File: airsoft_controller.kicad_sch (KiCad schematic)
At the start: 37 parts, among them J1 Conn_01x07, J2 Conn_01x03, J3 Conn_01x03, J4 Conn_01x01, J5 Conn_01x03, J6 Micro_SD_Card, J7 Conn_01x03, J8 Conn_01x02, SW1 MEMBRANE, SW2 MEMBRANE, SW3 MECH_SW, SW4 MEMBRANE, SW5 MEMBRANE, SW6 MEMBRANE, SW7 MEMBRANE, U1 CP2102N-Axx-xQFN20, U2 ESP32-S3-WROOM-1, U3 74HC595, U4 SN74HCS165

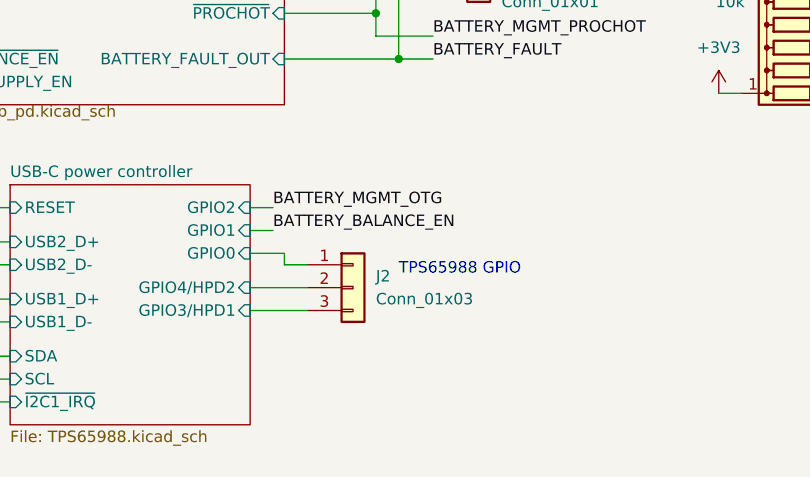
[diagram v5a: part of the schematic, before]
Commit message: edited usb pcb part
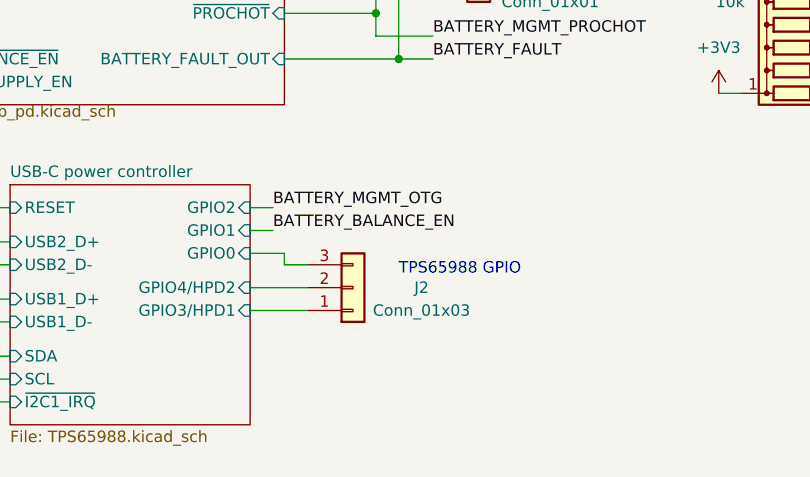
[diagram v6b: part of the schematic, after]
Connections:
- net USB-C power controller/GPIO0: now also J2.3 (Pin_3); no longer J2.1 (Pin_1)
- net USB-C power controller/GPIO3/HPD1: now also J2.1 (Pin_1); no longer J2.3 (Pin_3)
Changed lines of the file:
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@@
     (pin "1")
   )
-  (symbol (lib_id "Connector_Generic:Conn_01x03") (at 151.13 177.8 0) (unit 1)
-    (in_bom yes) (on_board yes) (fields_autoplaced)
-    (property "Reference" "J2" (id 0) (at 153.67 176.5299 0)
-      (effects (font (size 1.27 1.27)) (justify left))
-    )
-    (property "Value" "Conn_01x03" (id 1) (at 153.67 179.0699 0)
-      (effects (font (size 1.27 1.27)) (justify left))
-    )
+  (symbol (lib_id "Connector_Generic:Conn_01x03") (at 151.13 177.8 0) (mirror x) (unit 1)
+    (in_bom yes) (on_board yes)
+    (property "Reference" "J2" (id 0) (at 158.75 177.8 0))
+    (property "Value" "Conn_01x03" (id 1) (at 158.75 180.34 0))
     (property "Footprint" "Connector_PinSocket_2.54mm:PinSocket_1x03_P2.54mm_Vertical" (id 2) (at 151.13 177.8 0)
       (effects (font (size 1.27 1.27)) hide)
@@
     )
     (path "/dad78a3c-8763-4d20-b96b-942d6d484c24/f36f53a9-1291-4e1f-b242-7f104e919722"
-      (reference "C88") (unit 1) (value "10uF") (footprint "Capacitor_SMD:C_1206_3216Metric_Pad1.33x1.80mm_HandSolder")
+      (reference "C88") (unit 1) (value "10uF") (footprint "Capacitor_SMD:C_0805_2012Metric_Pad1.18x1.45mm_HandSolder")
     )
     (path "/dad78a3c-8763-4d20-b96b-942d6d484c24/d1db56bf-3f0a-4c29-8d97-5c6c3b7f42b1"
@@
     )
     (path "/dad78a3c-8763-4d20-b96b-942d6d484c24/7aaff0ab-8327-4583-8203-10eca9c35982"
-      (reference "C97") (unit 1) (value "10uF") (footprint "Capacitor_SMD:C_1206_3216Metric_Pad1.33x1.80mm_HandSolder")
+      (reference "C97") (unit 1) (value "10uF") (footprint "Capacitor_SMD:C_0805_2012Metric_Pad1.18x1.45mm_HandSolder")
     )
     (path "/dad78a3c-8763-4d20-b96b-942d6d484c24/4cd178db-9321-4997-91c7-f4d92beaf346"
@@
       (reference "C161") (unit 1) (value "22uF") (footprint "Capacitor_SMD:CP_Elec_5x5.3")
     )
+    (path "/dad78a3c-8763-4d20-b96b-942d6d484c24/2c870a98-ce2d-4021-953b-e874aa1f6f56"
+      (reference "C162") (unit 1) (value "4.7uF") (footprint "Capacitor_SMD:C_0603_1608Metric_Pad1.08x0.95mm_HandSolder")
+    )
     (path "/8ab84ef1-8252-469c-850a-9e4f14e4ddfd/384718a6-59f9-40f6-8b54-45db59321c91"

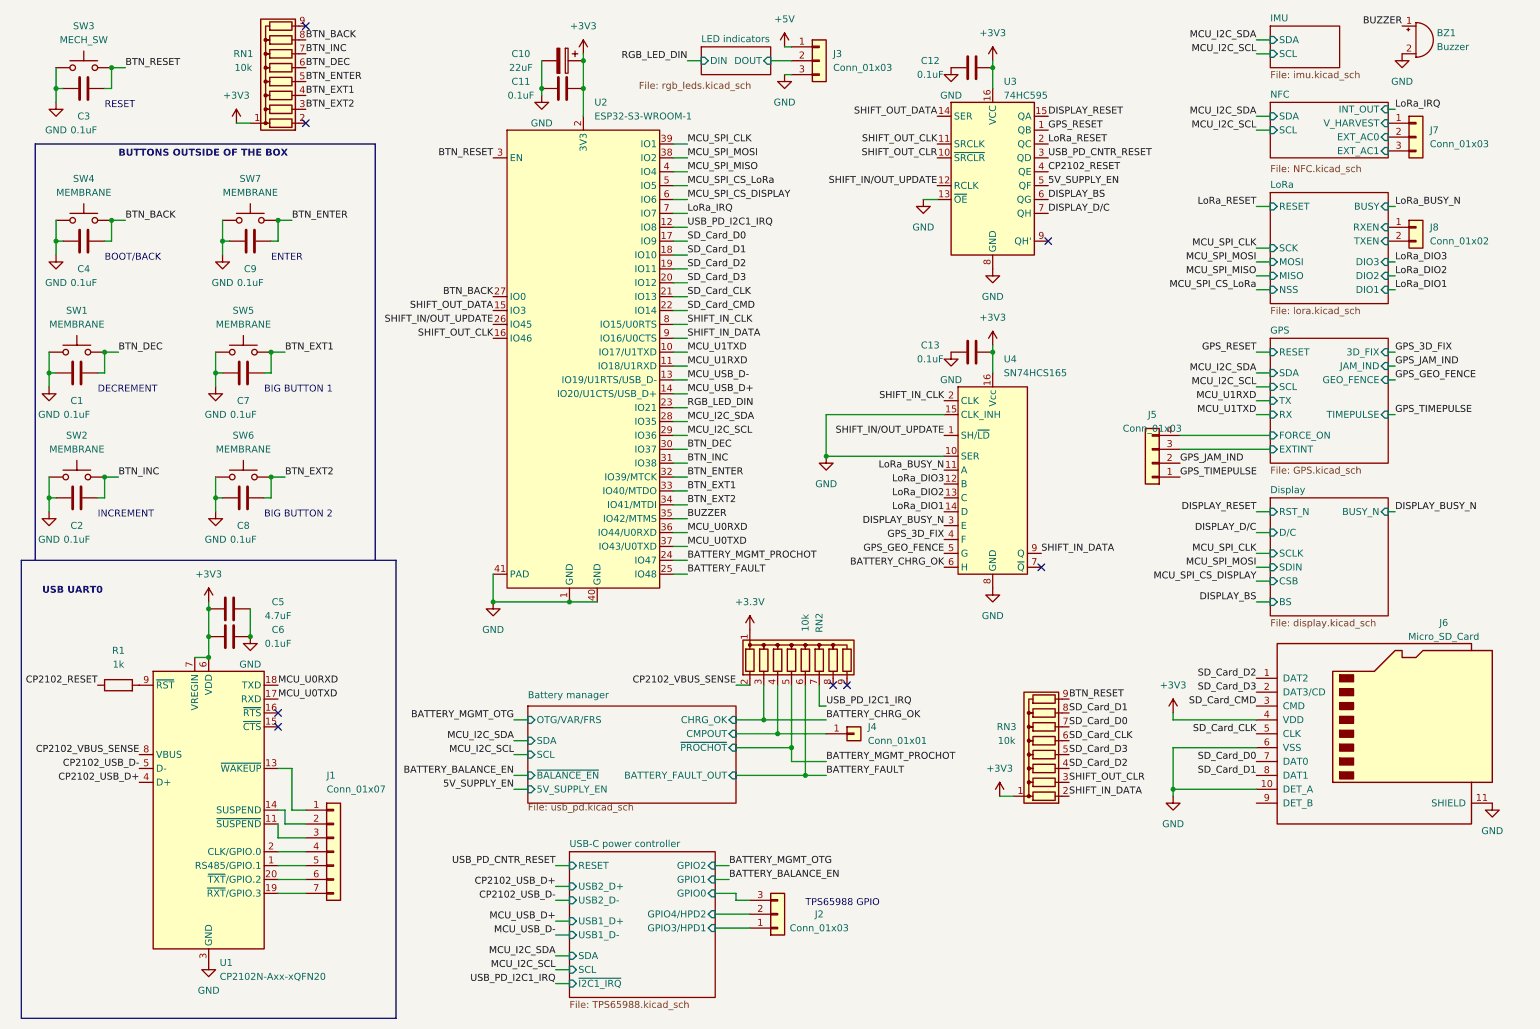
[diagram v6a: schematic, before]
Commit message: usb power source added, need to reassemble to 4-layers
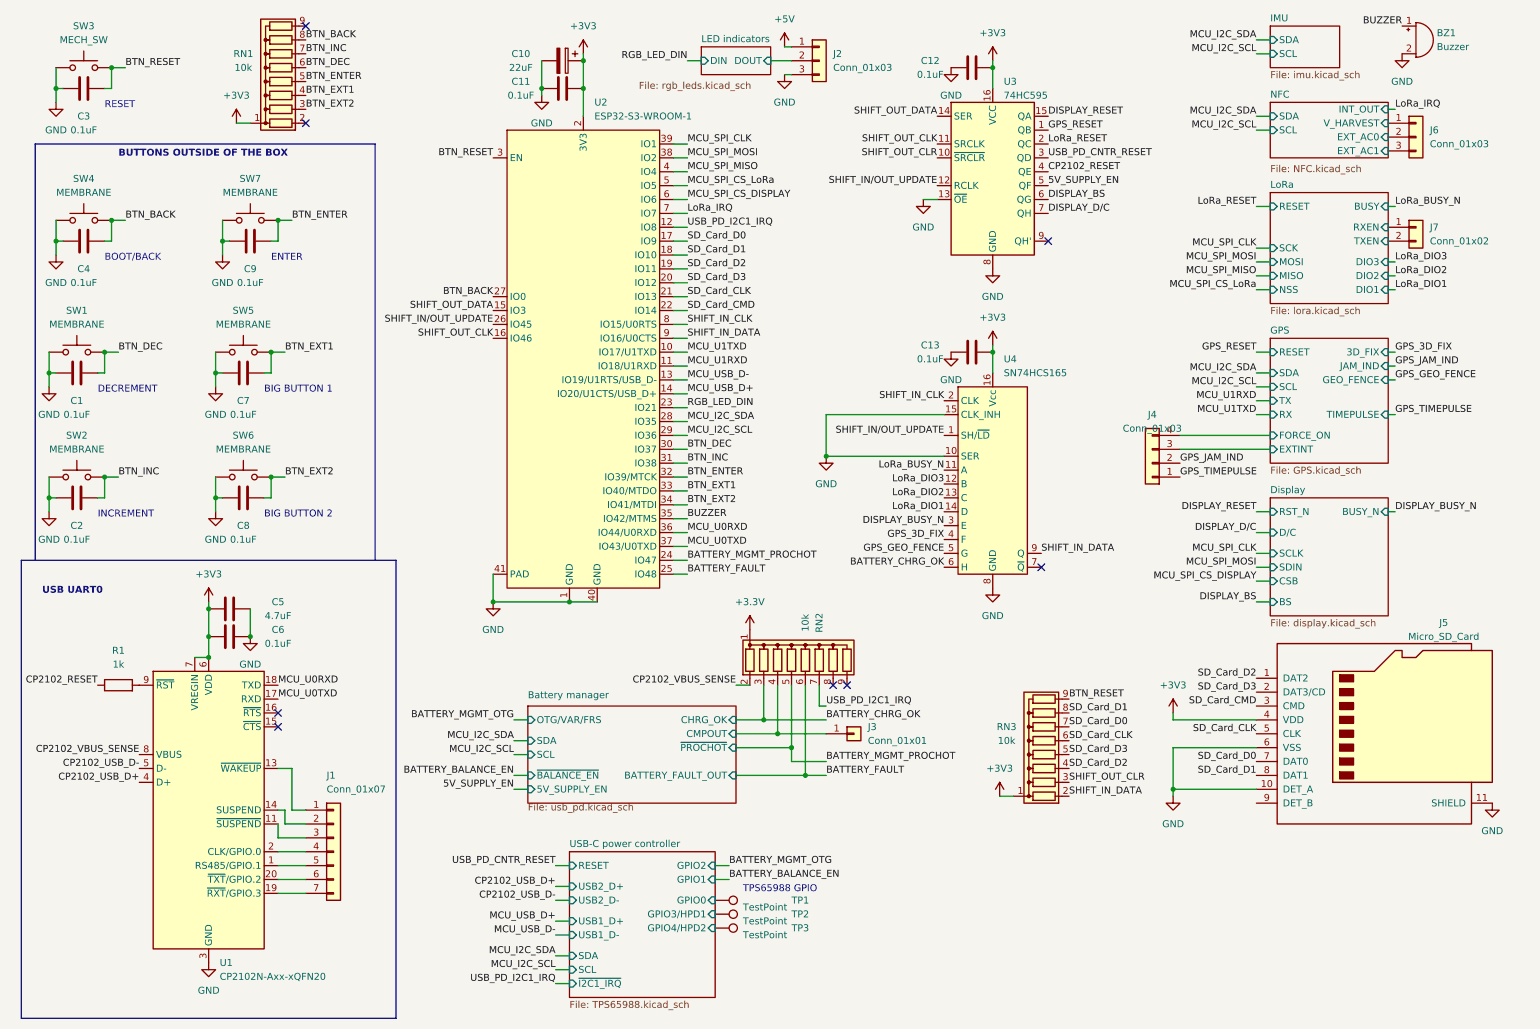
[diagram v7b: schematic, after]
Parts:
- removed J2: Conn_01x03, Connector_PinSocket_2.54mm:PinSocket_1x03_P2.54mm_Vertical, symbol Connector_Generic:Conn_01x03
- added TP1, TP2, TP3: TestPoint, TestPoint:TestPoint_Pad_D1.5mm, symbol Connector:TestPoint
- renumbered J3 to J2, J4 to J3, J5 to J4, J6 to J5, J7 to J6, J8 to J7
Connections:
- net USB-C power controller/GPIO0: now also TP1.1
- net USB-C power controller/GPIO3/HPD1: now also TP2.1
- net USB-C power controller/GPIO4/HPD2: now also TP3.1

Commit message: done first iteration of pcb routing, slikscreen still broken
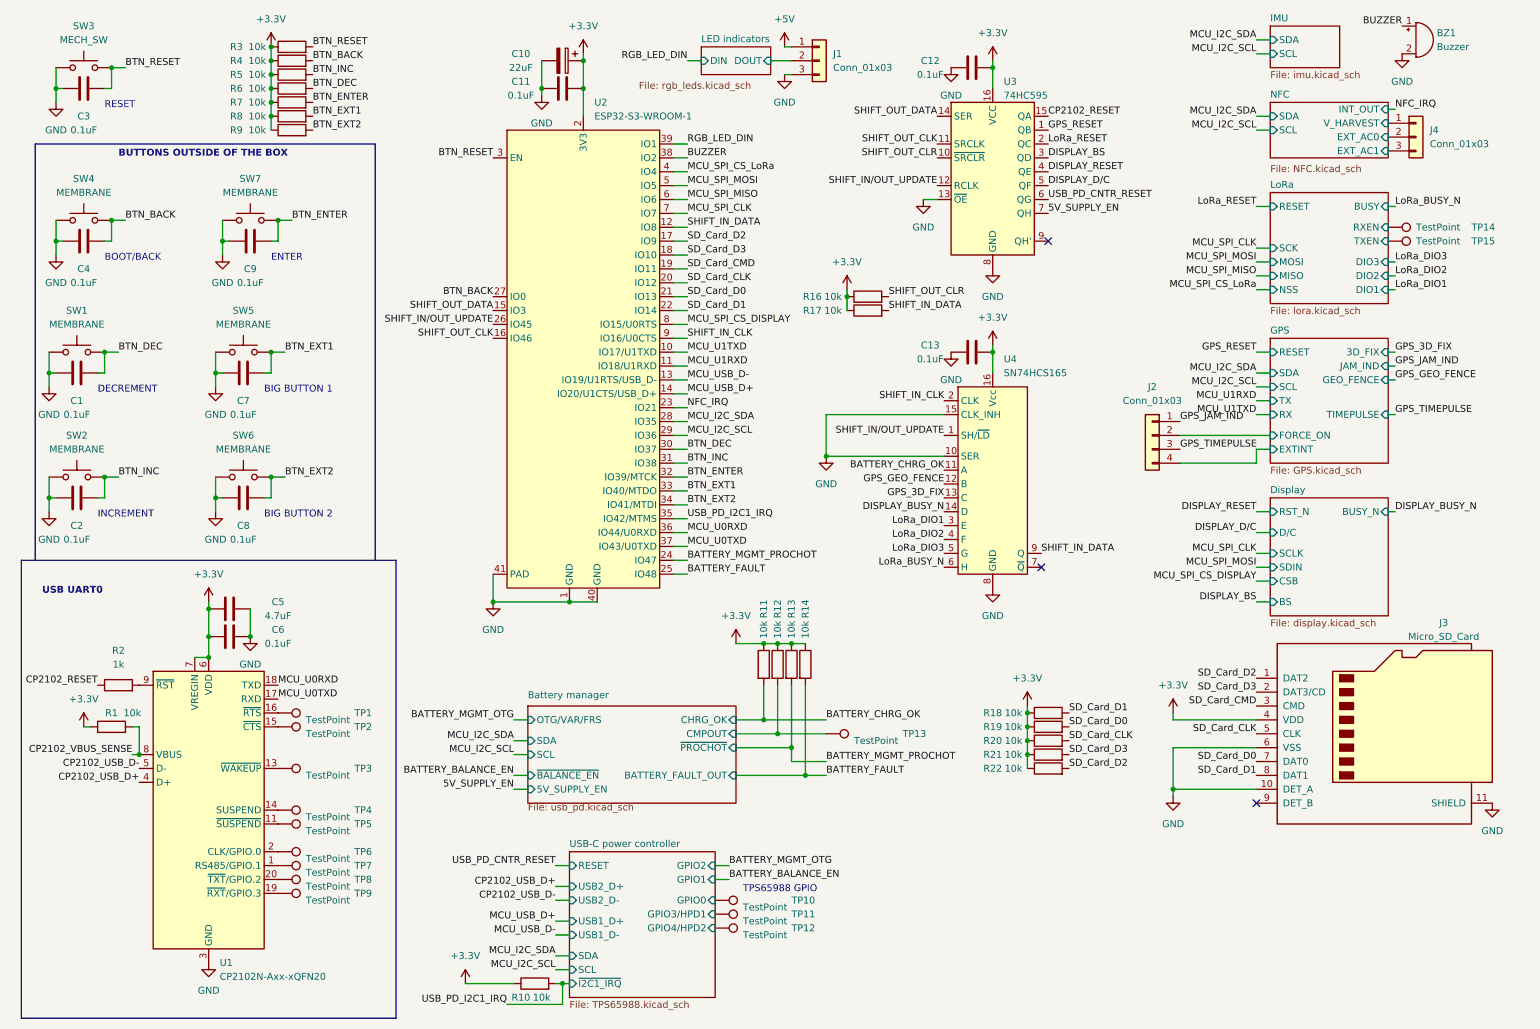
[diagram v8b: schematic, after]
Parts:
- removed J1: Conn_01x07, Connector_PinSocket_2.54mm:PinSocket_1x07_P2.54mm_Vertical, symbol Connector_Generic:Conn_01x07
- removed J3: Conn_01x01, Connector_PinSocket_2.54mm:PinSocket_1x01_P2.54mm_Vertical, symbol Connector_Generic:Conn_01x01
- removed J7: Conn_01x02, Connector_PinSocket_2.54mm:PinSocket_1x02_P2.54mm_Vertical, symbol Connector_Generic:Conn_01x02
- removed RN1, RN2, RN3: 10k, Resistor_THT:R_Array_SIP9, symbol Device:R_Network08
- added R1, R10, R11, R12, R13, R14, R16, R17, R18, R19, R20, R21, R22, R3, R4, R5, R6, R7, R8, R9: 10k, Resistor_SMD:R_0603_1608Metric_Pad0.98x0.95mm_HandSolder, symbol Device:R
- added TP1, TP13, TP14, TP15, TP2, TP3, TP4, TP5, TP6, TP7, TP8, TP9: TestPoint, TestPoint:TestPoint_Pad_D1.5mm, symbol Connector:TestPoint
- renumbered J2 to J1, J4 to J2, J5 to J3, J6 to J4, R1 to R2, TP1 to TP10, TP2 to TP11, TP3 to TP12
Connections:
- net +3V3 is gone; now on net +3.3V: C10.1, C11.2, C12.2, C13.2, C5.1, C6.1, J3.4 (VDD), U1.6 (VDD), U1.7 (VREGIN), U2.2 (3V3), U3.16 (VCC), U4.16 (Vcc)
- net LoRa_IRQ is gone; now on net MCU_SPI_CLK: U2.7 (IO7)
- net +3.3V: now also R1.1, R10.1, R11.1, R12.1, R13.1, R14.1, R16.1, R17.1, R18.1, R19.1, R20.1, R21.1, R22.1, R3.1, R4.1, R5.1, R6.1, R7.1, R8.1, R9.1
- net 5V_SUPPLY_EN: now also U3.7 (QH); no longer U3.5 (QF)
- net BATTERY_CHRG_OK: now also U4.11 (A), R11.2; no longer U4.6 (H)
- net BATTERY_FAULT: now also R14.2
- net BATTERY_MGMT_PROCHOT: now also R13.2
- net BTN_BACK: now also R4.2
- net BTN_DEC: now also R6.2
- net BTN_ENTER: now also R7.2
- net BTN_EXT1: now also R8.2
- net BTN_EXT2: now also R9.2
- net BTN_INC: now also R5.2
- net BTN_RESET: now also R3.2
- net BUZZER: now also U2.38 (IO2); no longer U2.35 (IO42/MTMS)
- net Battery manager/CMPOUT: now also R12.2, TP13.1
- net CP2102_RESET: now also U3.15 (QA); no longer U3.4 (QE)
- net CP2102_VBUS_SENSE: now also R1.2
- net DISPLAY_BS: now also U3.3 (QD); no longer U3.6 (QG)
- net DISPLAY_BUSY_N: now also U4.14 (D); no longer U4.3 (E)
- net DISPLAY_D/C: now also U3.5 (QF); no longer U3.7 (QH)
- net DISPLAY_RESET: now also U3.4 (QE); no longer U3.15 (QA)
- net GPS/EXTINT: now also J2.4 (Pin_4); no longer J2.3 (Pin_3)
- net GPS/FORCE_ON: now also J2.2 (Pin_2); no longer J2.4 (Pin_4)
- net GPS_3D_FIX: now also U4.13 (C); no longer U4.4 (F)
- net GPS_GEO_FENCE: now also U4.12 (B); no longer U4.5 (G)
- net GPS_JAM_IND: now also J2.1 (Pin_1); no longer J2.2 (Pin_2)
- net GPS_TIMEPULSE: now also J2.3 (Pin_3); no longer J2.1 (Pin_1)
- net LoRa/RXEN: now also TP14.1
- net LoRa/TXEN: now also TP15.1
- net LoRa_BUSY_N: now also U4.6 (H); no longer U4.11 (A)
- net LoRa_DIO1: now also U4.3 (E); no longer U4.14 (D)
- net LoRa_DIO2: now also U4.4 (F); no longer U4.13 (C)
- net LoRa_DIO3: now also U4.5 (G); no longer U4.12 (B)
- net MCU_SPI_CLK: no longer U2.39 (IO1)
- net MCU_SPI_CS_DISPLAY: now also U2.8 (IO15/U0RTS); no longer U2.6 (IO6)
- net MCU_SPI_CS_LoRa: now also U2.4 (IO4); no longer U2.5 (IO5)
- net MCU_SPI_MISO: now also U2.6 (IO6); no longer U2.4 (IO4)
- net MCU_SPI_MOSI: now also U2.5 (IO5); no longer U2.38 (IO2)
- net RGB_LED_DIN: now also U2.39 (IO1); no longer U2.23 (IO21)
- net SD_Card_CLK: now also U2.20 (IO12), R20.2; no longer U2.21 (IO13)
- net SD_Card_CMD: now also U2.19 (IO11); no longer U2.22 (IO14)
- net SD_Card_D0: now also U2.21 (IO13), R19.2; no longer U2.17 (IO9)
- net SD_Card_D1: now also U2.22 (IO14), R18.2; no longer U2.18 (IO10)
- net SD_Card_D2: now also U2.17 (IO9), R22.2; no longer U2.19 (IO11)
- net SD_Card_D3: now also U2.18 (IO10), R21.2; no longer U2.20 (IO12)
- net SHIFT_IN_CLK: now also U2.9 (IO16/U0CTS); no longer U2.8 (IO15/U0RTS)
- net SHIFT_IN_DATA: now also U2.12 (IO8), R17.2; no longer U2.9 (IO16/U0CTS)
- net SHIFT_OUT_CLR: now also R16.2
- net USB_PD_CNTR_RESET: now also U3.6 (QG); no longer U3.3 (QD)
- net USB_PD_I2C1_IRQ: now also U2.35 (IO42/MTMS), R10.2; no longer U2.12 (IO8)
- net at U1.13 (~{WAKEUP}): now also TP3.1
- net at U1.14 (SUSPEND): now also TP4.1
- net at U1.11 (~{SUSPEND}): now also TP5.1
- net at U1.2 (CLK/GPIO.0): now also TP6.1
- net at U1.1 (RS485/GPIO.1): now also TP7.1
- net at U1.20 (~{TXT}/GPIO.2): now also TP8.1
- net at U1.19 (~{RXT}/GPIO.3): now also TP9.1
- net at U1.15 (~{CTS}): now also TP2.1
- net at U1.16 (~{RTS}): now also TP1.1
- new net NFC_IRQ: U2.23 (IO21)
- no-connect marks 8 -> 3
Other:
- moved on the sheet: J2
